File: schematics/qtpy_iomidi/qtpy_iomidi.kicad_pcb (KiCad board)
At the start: 2 copper layers, 69.8 x 31.7 mm, 21 parts, among them J1 AudioJack4, J2 AudioJack4, J3 USB_A, J4 Conn_01x02_Pin, U2 H11L1

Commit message: some silkscreen
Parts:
- removed D2, D3: LED, LED_SMD:LED_0805_2012Metric
- added LED1: LED, LED_SMD:LED_0805_2012Metric, F.Cu at (47.3, 44.7)
- added LED2: LED, LED_SMD:LED_0805_2012Metric, F.Cu at (69.6, 44.7)
- added LED3: LED, LED_SMD:LED_0805_2012Metric, F.Cu at (79.9, 44.7)
- added R8: 1k, Resistor_SMD:R_0805_2012Metric, F.Cu at (42.9, 44.7)
- moved J4 0.51 mm to (53.8, 44.5)
- moved C1 0.41 mm to (60.7, 44.7)
- moved R6 0.25 mm to (65.3, 44.7)
- moved R7 0.25 mm to (75.4, 44.7)
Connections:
- U1 pad SCK: unconnected-(U1-PadSCK) -> /LED
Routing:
- net /LED: track 0.00 -> 19.3 mm
- net +3V3: track 96.8 -> 100.6 mm
- net Net-(LED1-A): track 0.00 -> 2.68 mm
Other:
- board text added: "5V Gnd"
- board text added: "IN"
- board text added: "MIDI TRS-A"
- board text added: "OUT"
- board text added: "QTPY RP2040"
- board text added: "USB HOST"
- board text added: "qtpy_iomidi"
- board text added: "qtpy_iomidi 10 May 2024 - @todbot github.com/todbot/qtpy_iomidi"

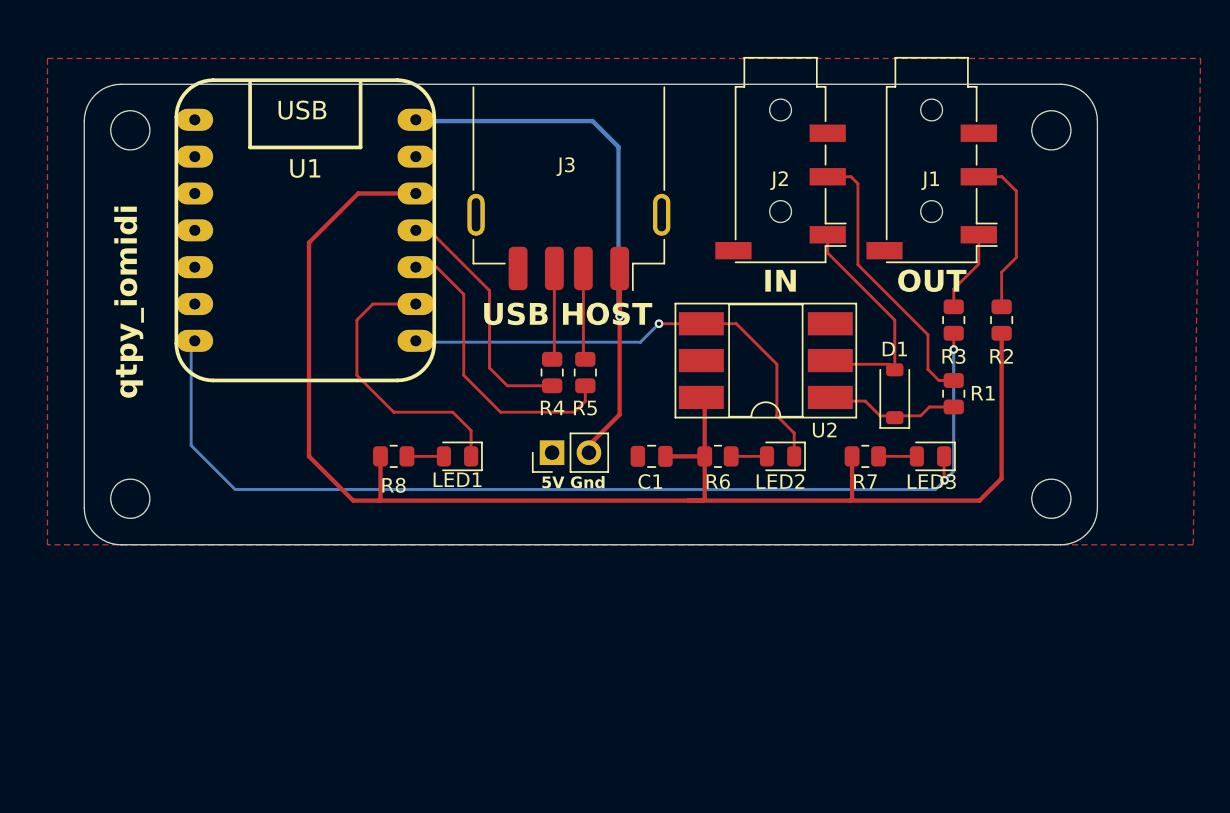
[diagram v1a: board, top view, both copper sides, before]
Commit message: switch to LCSC USB SMD host jack, add display & switch
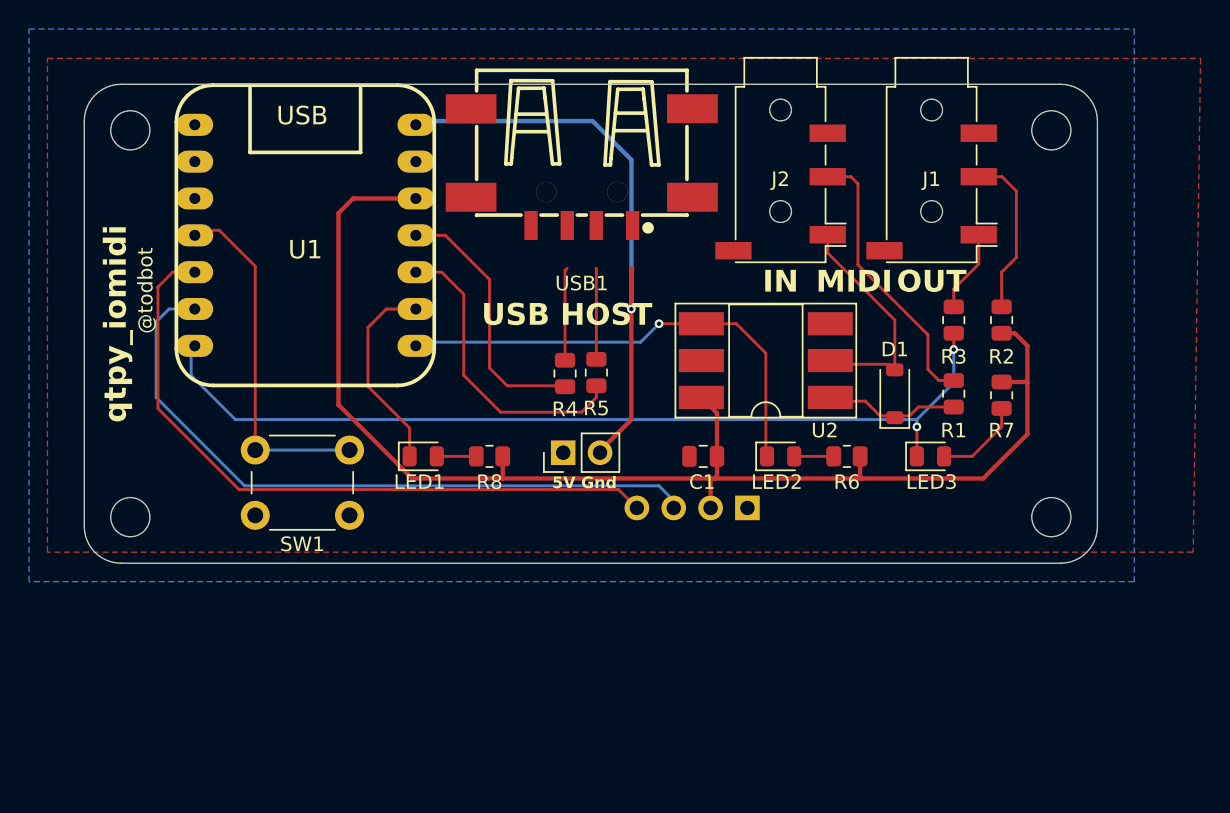
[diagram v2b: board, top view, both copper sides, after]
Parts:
- removed J3: USB_A, Connector_USB:USB_A_Receptacle_GCT_USB1046
- added J5: OLED-128x64, todbot_stuff:OLED-128x64-w_header, F.Cu at (63.5, 48.3)
- added SW1: SW_Omron_B3FS, Button_Switch_THT:SW_PUSH_6mm_H4.3mm, F.Cu at (39.9, 48.8)
- added USB1: 10.0 QTJ6.3, easyeda2kicad:USB-A-SMD_10.0-QTJ6.3, F.Cu at (55.9, 24.8)
- moved R7 10.3 mm to (84.8, 40.5), turned to 90 degrees
- moved R6 8.89 mm to (74.2, 44.7), turned to 0 degrees
- moved R8 6.60 mm to (49.5, 44.7), turned to 0 degrees
- moved C1 3.56 mm to (64.3, 44.7)
- moved LED1 2.36 mm to (45.0, 44.7), turned to 0 degrees
- moved H1 1.27 mm to (24.8, 48.9)
- moved H2 1.27 mm to (88.3, 48.9)
- moved R4 0.89 mm to (54.7, 39.0)
- moved J4 0.77 mm to (54.6, 44.5)
- moved R5 0.76 mm to (56.9, 38.9)
- moved U1 0.34 mm to (36.8, 29.5)
- turned LED2 to 0 degrees
- turned LED3 to 0 degrees
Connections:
- U1 pad A3: unconnected-(U1-PadA3) -> /SW
- U1 pad SCL: unconnected-(U1-PadSCL) -> /SCL
- U1 pad SDA: unconnected-(U1-PadSDA) -> /SDA
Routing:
- net /SCL: track 0.00 -> 47.4 mm
- net /SDA: track 0.00 -> 47.2 mm
- net /SW: track 0.00 -> 24.4 mm
- net /MIDI_OUT: track 72.9 -> 63.3 mm
- net +3V3: track 100.6 -> 91.1 mm
- net /LED: track 19.3 -> 13.9 mm
- net Net-(LED3-A): track 2.64 -> 6.19 mm
- net /USBH_D+: track 16.9 -> 18.2 mm
- net /MIDI_IN: track 33.5 -> 32.7 mm
- added copper zone on B.Cu, net GND
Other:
- board size 69.8 x 31.7 mm -> 69.8 x 33 mm
- board text added: "5V GND 3V MO MI SCK RX"
- board text added: "@todbot"
- board text added: "A0 A1 A2 A3 SDA SCL TX"
- board text added: "I2C OLED DISPLAY"
- board text added: "MIDI"
- board text added: "QTPY RP2040 XIAO RP2040"
- board text added: "gnd 3v3 scl sda"
- board text removed: "QTPY RP2040"

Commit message: pcb tweaks
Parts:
- moved R4 3.43 mm to (54.6, 35.6)
- moved R5 3.37 mm to (57.1, 35.6)
- moved J5 1.27 mm to (62.2, 48.3)
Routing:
- net VUSB: track 42.6 -> 46.8 mm
- net /USBH_D+: track 18.2 -> 14.1 mm
- net /USBH_D-: track 20.9 -> 18.6 mm
- net /SDA: track 47.2 -> 45.9 mm
- net /SCL: track 47.4 -> 46.3 mm
- net +3V3: track 91.1 -> 91.7 mm
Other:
- board text added: "I2C OLED DISP"

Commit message: more pcb tweaking
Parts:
- U1: footprint todbot_eagle2023:QTPY_TH -> todbot_eagle2023:QTPY_TH_HEADERSOCKET
- moved J4 3.81 mm to (54.6, 40.6)
- moved J5 1.27 mm to (61.0, 48.3)
- moved R5 0.51 mm to (56.6, 35.6)
- moved R4 0.25 mm to (54.4, 35.6)
- moved U1 0.25 mm to (36.6, 29.5)
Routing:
- net VUSB: track 46.8 -> 43.0 mm
- net /USBH_D-: track 18.6 -> 16.4 mm
- net /SCL: track 46.3 -> 44.3 mm
- net /SDA: track 45.9 -> 44.4 mm
- net +3V3: track 91.7 -> 92.7 mm

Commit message: added encoder
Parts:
- added SW2: RotaryEncoder_Switch, Rotary_Encoder:RotaryEncoder_Alps_EC11E-Switch_Vertical_H20mm_CircularMountingHoles, F.Cu at (38.8, 44.1)
- moved SW1 38.9 mm to (77.5, 58.4), turned to 90 degrees
- moved J5 10.2 mm to (61.0, 58.4)
- moved H1 9.55 mm to (24.1, 58.4)
- moved H2 9.52 mm to (88.3, 58.4)
- moved LED2 9.49 mm to (78.7, 47.2)
- moved LED3 5.75 mm to (85.1, 47.2)
- moved LED1 2.65 mm to (45.7, 47.2)
- moved R8 2.55 mm to (49.8, 47.2)
- moved R2 1.27 mm to (84.8, 36.6)
- moved R3 1.27 mm to (81.5, 36.6)
- moved U2 1.02 mm to (68.6, 39.1)
- moved D1 0.76 mm to (77.5, 41.1)
- moved J4 0.76 mm to (54.6, 41.4)
- moved R1 0.76 mm to (81.5, 41.1)
- moved R4 0.76 mm to (54.4, 36.3)
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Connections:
- U1 pad A0: unconnected-(U1-PadA0) -> /ENC_A
- U1 pad A1: unconnected-(U1-9-PadA1) -> /ENC_B
- U1 pad A2: unconnected-(U1-PadA2) -> /ENC_SW
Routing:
- net /SW: track 24.5 -> 89.5 mm
- net /ENC_SW: track 0.00 -> 34.9 mm
- net /ENC_A: track 0.00 -> 28.2 mm
- net /ENC_B: track 0.00 -> 23.2 mm
- net +3V3: track 92.7 -> 112.6 mm, vias 0 -> 2
- net /SDA: track 44.4 -> 59.3 mm
- net /MIDI_IN: track 32.7 -> 44.0 mm
- net /SCL: track 44.3 -> 55.1 mm
- net VUSB: track 43.0 -> 38.1 mm
- net /MIDI_OUT: track 63.3 -> 68.2 mm
- net /LED: track 13.7 -> 16.9 mm
- net Net-(LED2-A): track 2.72 -> 5.42 mm
- net Net-(J1-PadR1): track 11.4 -> 13.3 mm
- net Net-(J1-PadT): track 5.68 -> 6.95 mm
- net Net-(USB1-D-): track 5.97 -> 6.73 mm
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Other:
- board size 69.8 x 33 mm -> 69.8 x 43.2 mm
- board text added: "PUSH!"
- board text added: "RX MIDI TX"
- board text added: "USB MIDI"

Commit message: submit to fab
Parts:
- moved H1 0.90 mm to (24.8, 59.1)
- moved R4 0.76 mm to (55.1, 36.3)
- moved H2 0.63 mm to (88.3, 59.1)
- moved R5 0.51 mm to (57.1, 36.3)
- moved J1 0.25 mm to (80.3, 25.6)
- moved J2 0.25 mm to (69.8, 25.6)
- moved USB1 0.24 mm to (56.1, 24.8)
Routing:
- net Net-(J1-PadT): track 6.95 -> 7.78 mm
- net /USBH_D+: track 13.4 -> 14.1 mm
- net /USBH_D-: track 16.1 -> 16.6 mm
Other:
- outline, holes or cut-outs redrawn
- board text added: "IN MIDI OUT"
- board text added: "JLCJLCJLCJLC"
- board text removed: "RX MIDI TX"

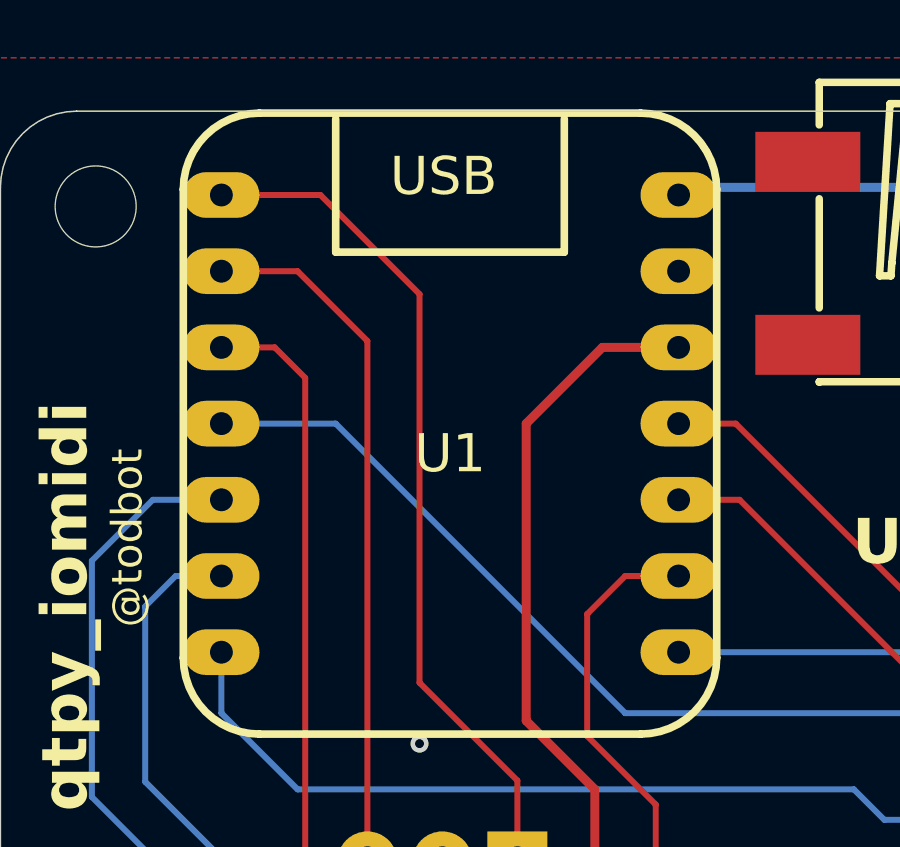
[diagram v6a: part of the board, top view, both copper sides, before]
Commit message: qtpy holes too small, fixed I think
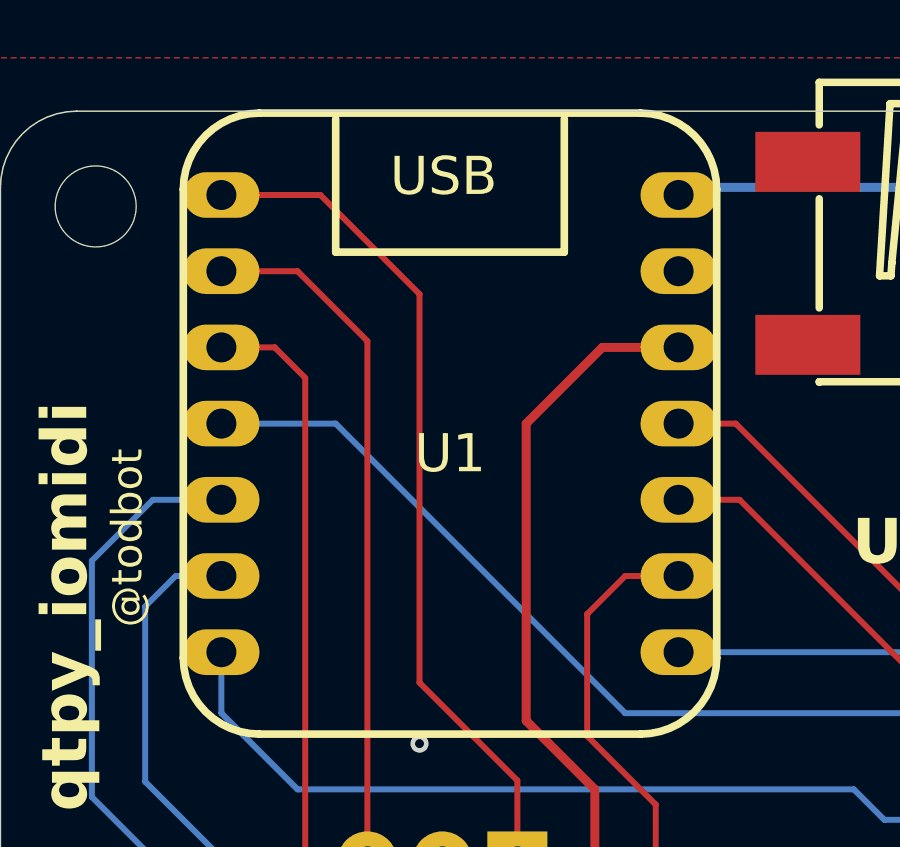
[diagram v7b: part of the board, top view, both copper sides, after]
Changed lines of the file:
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@@
 			)
 		)
+		(property "LCSC" "C431535"
+			(at 0 0 -90)
+			(unlocked yes)
+			(layer "F.Fab")
+			(hide yes)
+			(effects
+				(font
+					(size 1 1)
+					(thickness 0.15)
+				)
+			)
+		)
 		(property ki_fp_filters "Jack*")
 		(sheetname "Root")
@@
 			(at 7.62 -2.54)
 			(size 2.54 1.524)
-			(drill 0.762)
+			(drill 1)
 			(layers "*.Cu" "*.Mask")
 			(remove_unused_layers no)
@@
 			(at 7.62 -7.62)
 			(size 2.54 1.524)
-			(drill 0.762)
+			(drill 1)
 			(layers "*.Cu" "*.Mask")
 			(remove_unused_layers no)
@@
 			(at -7.62 -7.62)
 			(size 2.54 1.524)
-			(drill 0.762)
+			(drill 1)
 			(layers "*.Cu" "*.Mask")
 			(remove_unused_layers no)
@@
 			(at -7.62 -5.08)
 			(size 2.54 1.524)
-			(drill 0.762)
+			(drill 1)
 			(layers "*.Cu" "*.Mask")
 			(remove_unused_layers no)
@@
 			(at -7.62 -2.54)
 			(size 2.54 1.524)
-			(drill 0.762)
+			(drill 1)
 			(layers "*.Cu" "*.Mask")
 			(remove_unused_layers no)
@@
 			(at -7.62 0)
 			(size 2.54 1.524)
-			(drill 0.762)
+			(drill 1)
 			(layers "*.Cu" "*.Mask")
 			(remove_unused_layers no)
@@
 			(at 7.62 -5.08)
 			(size 2.54 1.524)
-			(drill 0.762)
+			(drill 1)
 			(layers "*.Cu" "*.Mask")
 			(remove_unused_layers no)
@@
 			(at 7.62 2.54)
 			(size 2.54 1.524)
-			(drill 0.762)
+			(drill 1)
 			(layers "*.Cu" "*.Mask")
 			(remove_unused_layers no)
@@
 			(at 7.62 0)
 			(size 2.54 1.524)
-			(drill 0.762)
+			(drill 1)
 			(layers "*.Cu" "*.Mask")
 			(remove_unused_layers no)
@@
 			(at 7.62 7.62)
 			(size 2.54 1.524)
-			(drill 0.762)
+			(drill 1)
 			(layers "*.Cu" "*.Mask")
 			(remove_unused_layers no)
@@
 			(at 7.62 5.08)
 			(size 2.54 1.524)
-			(drill 0.762)
+			(drill 1)
 			(layers "*.Cu" "*.Mask")
 			(remove_unused_layers no)
@@
 			(at -7.62 5.08)
 			(size 2.54 1.524)
-			(drill 0.762)
+			(drill 1)
 			(layers "*.Cu" "*.Mask")
 			(remove_unused_layers no)
@@
 			(at -7.62 2.54)
 			(size 2.54 1.524)
-			(drill 0.762)
+			(drill 1)
 			(layers "*.Cu" "*.Mask")
 			(remove_unused_layers no)
@@
 			(at -7.62 7.62)
 			(size 2.54 1.524)
-			(drill 0.762)
+			(drill 1)
 			(layers "*.Cu" "*.Mask")
 			(remove_unused_layers no)
@@
 			)
 		)
+		(property "LCSC" "C431535"
+			(at 0 0 -90)
+			(unlocked yes)
+			(layer "F.Fab")
+			(hide yes)
+			(effects
+				(font
+					(size 1 1)
+					(thickness 0.15)
+				)
+			)
+		)
 		(property ki_fp_filters "Jack*")
 		(sheetname "Root")
@@
 			)
 		)
+		(property "LCSC" "C78589"
+			(at 0 0 180)
+			(unlocked yes)
+			(layer "F.Fab")
+			(hide yes)
+			(effects
+				(font
+					(size 1 1)
+					(thickness 0.15)
+				)
+			)
+		)
 		(property ki_fp_filters "DIP*W7.62mm* DIP*W10.16mm* SMDIP*W9.53mm*")
 		(sheetname "Root")
@@
 			)
 		)
-		(property "Description" "Light emitting diode"
+		(property "Description" "Light emitting diode, green"
 			(at 0 0 0)
 			(unlocked yes)
@@
 			)
 		)
+		(property "LCSC" "C49678"
+			(at 0 0 0)
+			(unlocked yes)
+			(layer "F.Fab")
+			(hide yes)
+			(effects
+				(font
+					(size 1 1)
+					(thickness 0.15)
+				)
+			)
+		)
 		(property ki_fp_filters "LED* LED_SMD:* LED_THT:*")
 		(sheetname "Root")
@@
 		(tags "LED")
 		(property "Reference" "LED1"
-			(at -0.254 1.778 360)
+			(at -0.254 1.778 0)
 			(layer "F.SilkS")
 			(hide yes)
@@
 		)
 		(property "Value" "LED"
-			(at 0 1.65 360)
+			(at 0 1.65 0)
 			(layer "F.Fab")
 			(effects
@@
 			)
 		)
-		(property "Description" "Light emitting diode"
+		(property "Description" "Light emitting diode, green"
 			(at 0 0 0)
 			(unlocked yes)
@@
 			)
 		)
+		(property "LCSC" "C49678"
+			(at 0 0 0)
+			(unlocked yes)
+			(layer "F.Fab")
+			(hide yes)
+			(effects
+				(font
+					(size 1 1)
+					(thickness 0.15)
+				)
+			)
+		)
 		(property ki_fp_filters "LED* LED_SMD:* LED_THT:*")
 		(sheetname "Root")
@@
 		)
 		(fp_text user "${REFERENCE}"
-			(at 0 0 360)
+			(at 0 0 0)
 			(layer "F.Fab")
 			(effects
@@
 			)
 		)
-		(property "Description" "Light emitting diode"
+		(property "Description" "Light emitting diode, green"
 			(at 0 0 0)
 			(unlocked yes)
@@
 			)
 		)
+		(property "LCSC" "C49678"
+			(at 0 0 0)
+			(unlocked yes)
+			(layer "F.Fab")
+			(hide yes)
+			(effects
+				(font
+					(size 1 1)
+					(thickness 0.15)
+				)
+			)
+		)
 		(property ki_fp_filters "LED* LED_SMD:* LED_THT:*")
 		(sheetname "Root")
@@
 		(tags "capacitor")
 		(property "Reference" "C1"
-			(at 2.794 0 360)
+			(at 2.794 0 0)
 			(layer "F.SilkS")
 			(effects
@@
 		)
 		(property "Value" "100n"
-			(at 0 1.679999 360)
+			(at 0 1.679999 0)
 			(layer "F.Fab")
 			(effects
@@
 		)
 		(fp_text user "${REFERENCE}"
-			(at 0 0 360)
+			(at 0 0 0)
 			(layer "F.Fab")
 			(effects
@@
 		(tags "resistor")
 		(property "Reference" "R8"
-			(at 2.54 0 360)
+			(at 2.54 0 0)
 			(layer "F.SilkS")
 			(effects
@@
 		)
 		(property "Value" "1k"
-			(at 0 1.65 360)
+			(at 0 1.65 0)
 			(layer "F.Fab")
 			(effects
@@
 		)
 		(fp_text user "${REFERENCE}"
-			(at 0 0 360)
+			(at 0 0 0)
 			(layer "F.Fab")
 			(effects
@@
 		(tags "tact sw push 6mm")
 		(property "Reference" "SW1"
-			(at 3.25 2.25 270)
+			(at 3.25 2.25 -90)
 			(layer "F.SilkS")
 			(effects
@@
 		)
 		(property "Value" "SW_Omron_B3FS"
-			(at 2.996 2.25 270)
+			(at 2.996 2.25 -90)
 			(layer "F.Fab")
 			(effects
@@
 		)
 		(fp_text user "${REFERENCE}"
-			(at 3.25 2.25 270)
+			(at 3.25 2.25 -90)
 			(layer "F.Fab")
 			(effects
